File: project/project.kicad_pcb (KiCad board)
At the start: 4 copper layers, 84 x 41 mm, 98 parts, among them J101 BUS, J102 BUS, J103 Back, J201 24V, J202 5V, J203 3V3, J204 6V, J301 USB_C_Receptacle_USB2.0, Q201 MMBT3904, SW301 15mm, SW302 15mm, U101 GX101, U201 LW6550A23E, U202 MT3406, U203 ME3121AM6G, U301 USBLC6-2SC6, U302 esp32-C3FH4X, U303 XL1050, Y301 40MHz

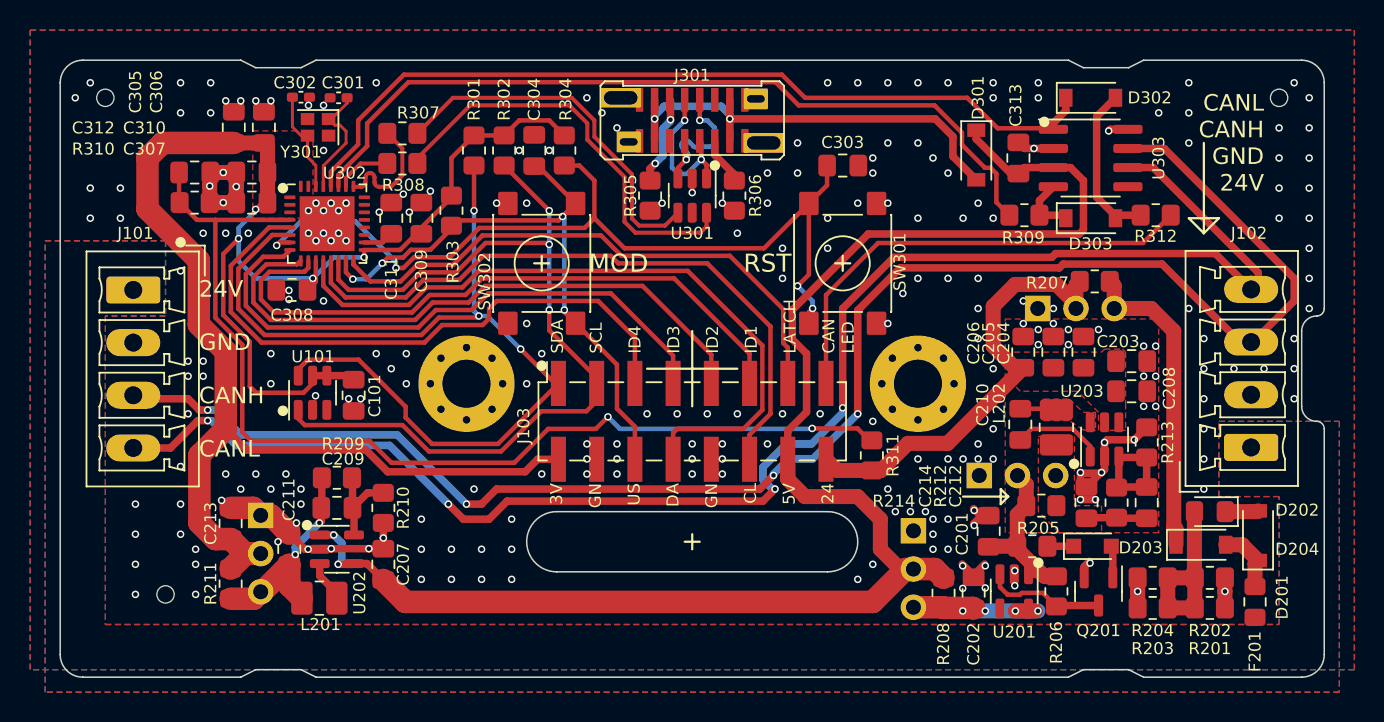
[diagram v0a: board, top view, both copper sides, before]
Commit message: fixes after preliminary testing
* Switching to TMP102 as TMP101 is no longer available
* Removing 5V LDO with OVP as it caused more problems
* bumping up version
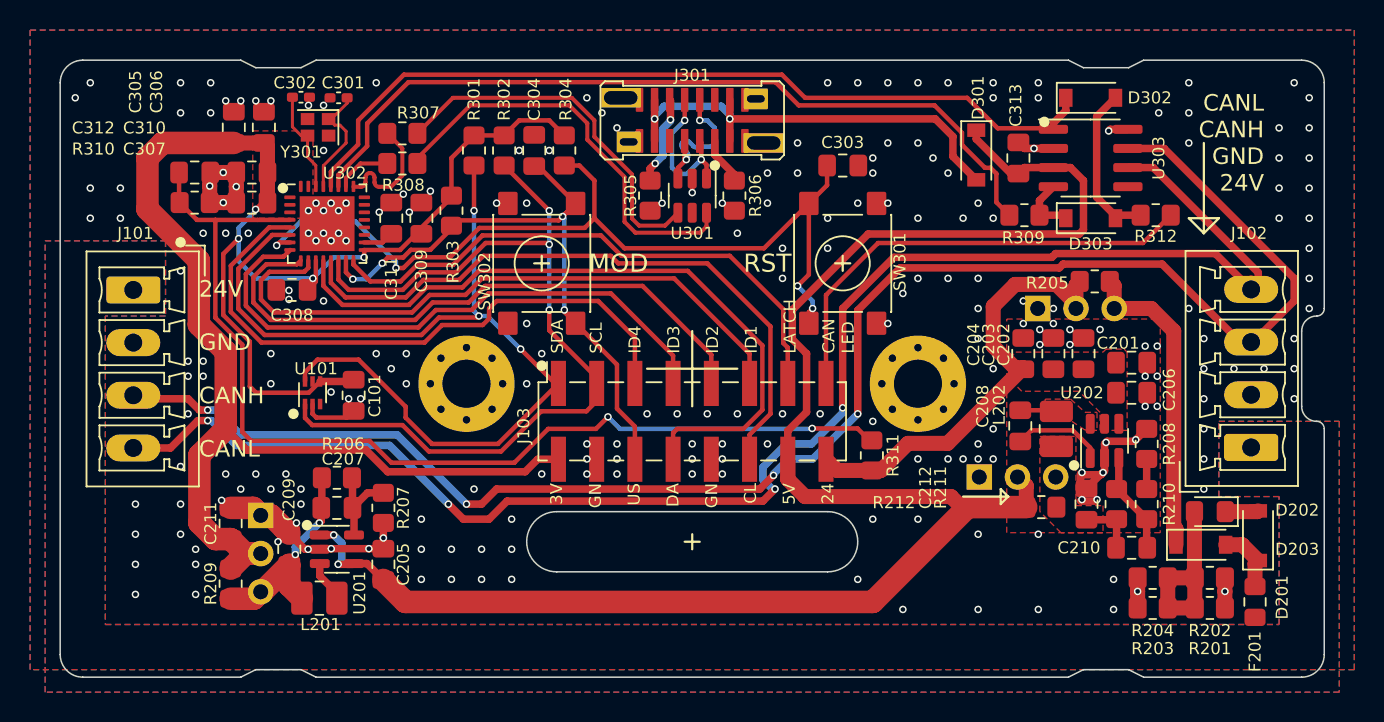
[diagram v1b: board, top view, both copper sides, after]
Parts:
- removed the C201 at (188.0, 144.8)
- removed the C202 at (187.0, 148.9)
- removed the D203 at (194.9, 145.8)
- removed the J202 at (183.0, 144.8)
- removed Q201: MMBT3904, Package_TO_SOT_SMD:SOT-23
- removed the R205 at (190.9, 145.8)
- removed the R206 at (192.5, 148.8)
- removed R213: 22k, Resistor_SMD:R_0805_2012Metric_Pad1.20x1.40mm_HandSolder
- removed REF** (x3): toolhole, -local:toolhole
- removed the U201 at (189.7, 148.8)
- removed kibuzzard-68F6C8CD: G***, kibuzzard-68F6C8CD
- removed kibuzzard-698AF992: G***, kibuzzard-698AF992
- removed kibuzzard-698C36BD: G***, kibuzzard-698C36BD
- added R210: 10k, Resistor_SMD:R_0805_2012Metric_Pad1.20x1.40mm_HandSolder, F.Cu at (198.5, 143.0)
- added kibuzzard-69BC7741: G***, kibuzzard-69BC7741, B.Cu at (189.3, 152.5)
- added kibuzzard-69BC7F29: G***, kibuzzard-69BC7F29, B.Cu at (183.8, 141.5)
- R208: value 0R1 -> 10k
- R211: renamed from R212; value 200k -> 150k
- U101: value GX101 -> TMP102; footprint Package_TO_SOT_SMD:SOT-23-6 -> -local:SOT-563
- moved R208 16.7 mm to (198.5, 139.0)
- moved C210 3.16 mm to (197.5, 145.9), turned to 180 degrees
- moved J203 0.10 mm to (187.3, 141.2)
- moved R212 0.10 mm to (191.5, 143.2)
- moved C201 0.10 mm to (197.5, 133.6)
- moved C202 0.10 mm to (194.3, 133.0)
- moved C203 0.10 mm to (192.3, 133.0)
- moved C204 0.10 mm to (190.3, 133.0)
- moved C206 0.10 mm to (197.5, 135.6)
- moved C208 0.10 mm to (190.1, 137.8)
- moved C212 0.10 mm to (194.5, 143.0)
- moved L202 0.10 mm to (192.5, 138.0)
- moved R211 0.10 mm to (196.5, 143.0)
- moved U202 0.10 mm to (195.7, 138.8)
- renumbered C203 to C201, C204 to C202, C205 to C203, C206 to C204, C207 to C205, C208 to C206, C209 to C207, C210 to C208, C211 to C209, C212 to C210, C213 to C211, C214 to C212, D204 to D203, J203 to J202, J204 to J203, R207 to R205, R209 to R206, R210 to R207, R211 to R209, R214 to R212, U202 to U201, U203 to U202
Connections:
- C210 pad 2: /PSU/VO6 -> /PSU/VO5
- C212 pad 1: /PSU/VO6 -> /PSU/VO5
- J203 pad 2: /PSU/6V -> 5V
- J203 pad 3: /PSU/VO6 -> /PSU/VO5
- L202 pad 2: /PSU/VO6 -> /PSU/VO5
- R208 pad 1: 5V -> GND
- R208 pad 2: /PSU/VO5 -> Net-(R208-Pad2)
- R211 pad 2: /PSU/VO6 -> /PSU/VO5
- R212 pad 1: /PSU/6V -> 5V
- R212 pad 2: /PSU/VO6 -> /PSU/VO5
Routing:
- net /PSU/6V: track 14.7 -> 0.00 mm
- net 5V: track 103.8 -> 113.8 mm
- net /PSU/EN: track 8.06 -> 0.00 mm
- net /PSU/VO5: track 10.4 -> 3.93 mm, vias 4 -> 0
- net /PSU/VO6: track 4.03 -> 0.00 mm
- net GND: track 45.5 -> 43.2 mm, vias 247 -> 237
- net /PSU/BASE: track 2.10 -> 0.00 mm
- net Net-(R208-Pad2): track 0.00 -> 2.00 mm
- net /PSU/BASE_UP: track 1.75 -> 0.00 mm
- net /PSU/FB: track 7.98 -> 6.87 mm
- net 3V3: track 126.2 -> 125.7 mm
- added copper zone on F.Cu, net /PSU/VO5
- removed copper zone on F.Cu, net /PSU/VO6

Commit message: fixing tmp102 pinout
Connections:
- U101 pad 4: 3V3 -> SDA
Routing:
- net SDA: track 63.8 -> 64.9 mm
- net 3V3: track 125.7 -> 126.4 mm
- net GND: vias 237 -> 236
